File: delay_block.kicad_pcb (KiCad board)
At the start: 2 copper layers, 55.4 x 81.8 mm, 51 parts, among them J1 Conn_Coaxial, J2 Conn_Coaxial, J3 Conn_Coaxial, J4 Conn_Coaxial, J5 Conn_Coaxial, J6 Conn_Coaxial, J7 Conn_Coaxial, J8 Conn_Coaxial, J9 Screw_Terminal_01x02, U1 DS1100Z-500+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

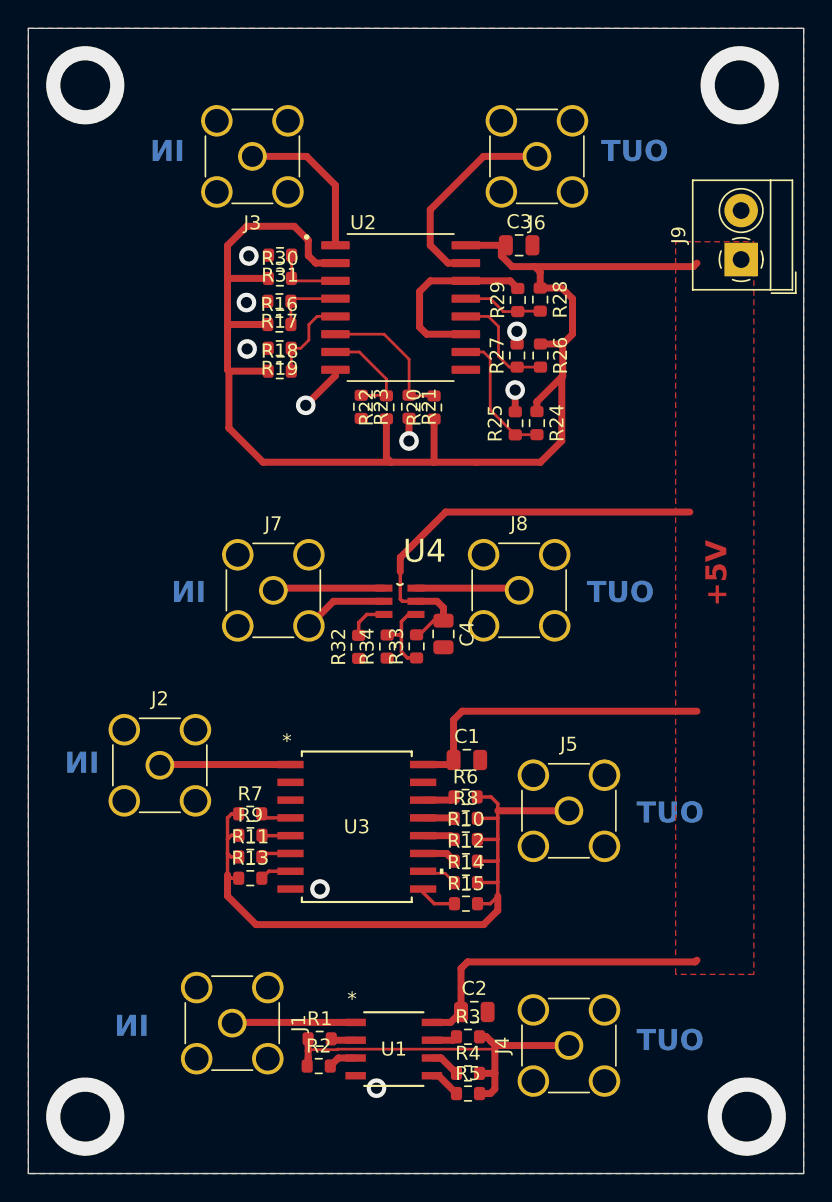
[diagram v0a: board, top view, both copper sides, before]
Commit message: hardwired jumpers to set ~500us everywhere
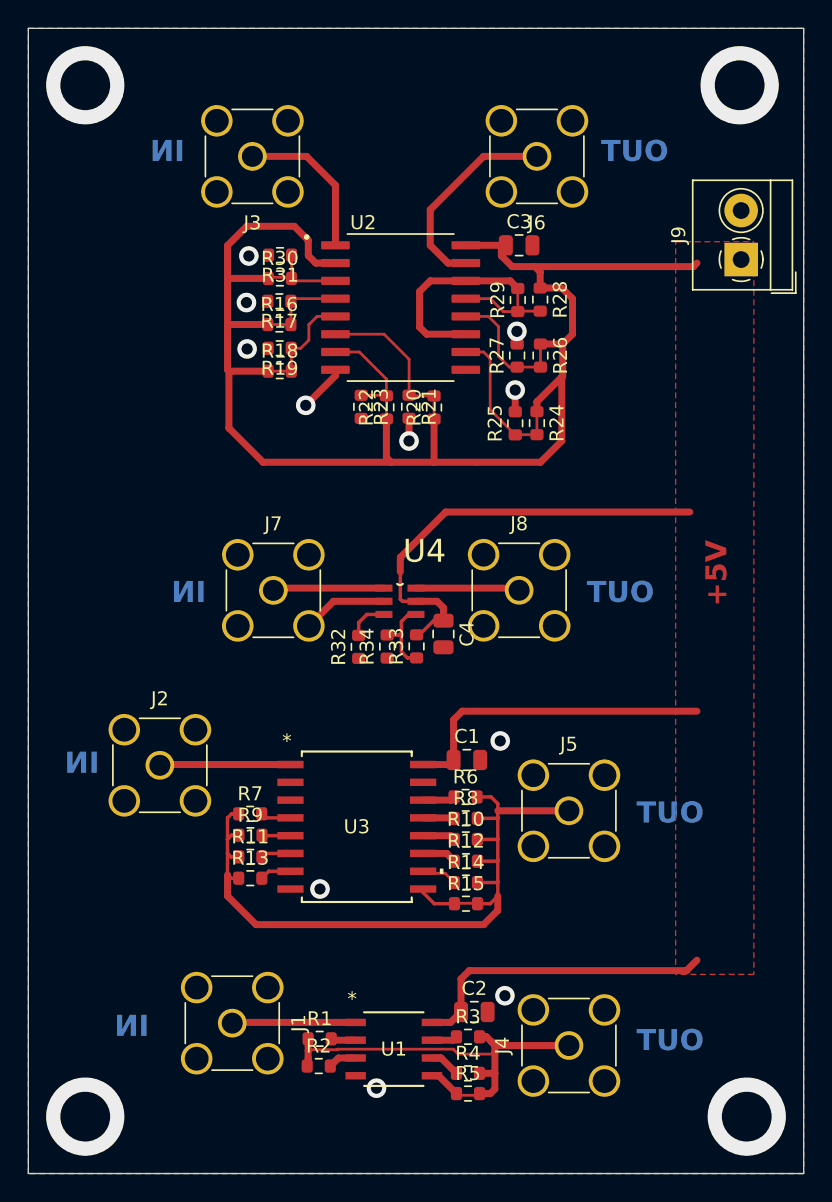
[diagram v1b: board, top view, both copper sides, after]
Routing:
- net GND: vias 13 -> 15
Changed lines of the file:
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@@
 		)
+	)
+	(gr_line
+		(start 106.193742 91.315606)
+		(end 106.188841 89.839156)
+		(stroke
+			(width 0.2)
+			(type default)
+		)
+		(layer "F.Cu")
+	)
+	(gr_line
+		(start 94.433714 87.98479)
+		(end 95.910164 87.979889)
+		(stroke
+			(width 0.2)
+			(type default)
+		)
+		(layer "F.Cu")
+	)
+	(gr_line
+		(start 107.696 139.7)
+		(end 109.728 139.7)
+		(stroke
+			(width 0.2)
+			(type default)
+		)
+		(layer "F.Cu")
+	)
+	(gr_line
+		(start 107.696 125.984)
+		(end 109.22 125.984)
+		(stroke
+			(width 0.2)
+			(type default)
+		)
+		(layer "F.Cu")
+	)
+	(gr_line
+		(start 112.171951 83.640874)
+		(end 112.16705 82.164424)
+		(stroke
+			(width 0.2)
+			(type default)
+		)
+		(layer "F.Cu")
+	)
+	(gr_line
+		(start 113.54045 92.432225)
+		(end 113.535549 90.955775)
+		(stroke
+			(width 0.2)
+			(type default)
+		)
+		(layer "F.Cu")
+	)
+	(gr_line
+		(start 113.79445 87.606225)
+		(end 113.789549 86.129775)
+		(stroke
+			(width 0.2)
+			(type default)
+		)
+		(layer "F.Cu")
+	)
+	(gr_line
+		(start 94.403323 84.65273)
+		(end 95.879773 84.647829)
+		(stroke
+			(width 0.2)
+			(type default)
+		)
+		(layer "F.Cu")
+	)
+	(gr_line
+		(start 94.488 81.28)
+		(end 95.96445 81.275099)
+		(stroke
+			(width 0.2)
+			(type default)
+		)
+		(layer "F.Cu")
+	)
+	(gr_line
+		(start 102.789702 91.305102)
+		(end 102.784801 89.828652)
+		(stroke
+			(width 0.2)
+			(type default)
+		)
+		(layer "F.Cu")
 	)
 	(gr_rect
@@
 	)
 	(via
+		(at 111.252 132.588)
+		(size 1.4)
+		(drill 0.8)
+		(layers "F.Cu" "B.Cu")
+		(free yes)
+		(net 5)
+	)
+	(via
 		(at 104.404031 92.968017)
 		(size 1.4)
@@
 	)
 	(via
+		(at 110.917719 114.392297)
+		(size 1.4)
+		(drill 0.8)
+		(layers "F.Cu" "B.Cu")
+		(free yes)
+		(net 5)
+	)
+	(via
 		(at 128.016 67.564)
 		(size 5.588)
@@
 	)
 	(segment
+		(start 108.712 130.795203)
+		(end 124.220797 130.795203)
+		(width 0.5)
+		(layer "F.Cu")
+		(net 6)
+	)
+	(segment
 		(start 91.520515 81.360515)
 		(end 91.44 81.28)
@@
 	)
 	(segment
-		(start 108.116192 130.643808)
-		(end 108.586202 130.173798)
-		(width 0.5)
-		(layer "F.Cu")
-		(net 6)
-	)
-	(segment
 		(start 115.319944 82.045944)
 		(end 113.772173 82.045944)
@@
 	)
 	(segment
+		(start 108.116192 133.749203)
+		(end 108.116192 131.391011)
+		(width 0.5)
+		(layer "F.Cu")
+		(net 6)
+	)
+	(segment
 		(start 91.44 84.836)
 		(end 91.44 83.82)
@@
 	)
 	(segment
+		(start 108.116192 131.391011)
+		(end 108.712 130.795203)
+		(width 0.5)
+		(layer "F.Cu")
+		(net 6)
+	)
+	(segment
 		(start 105.41 116.078)
 		(end 107.25909 116.078)
@@
 	)
 	(segment
-		(start 124.842202 130.173798)
+		(start 124.220797 130.795203)
 		(end 124.968 130.048)
 		(width 0.5)
@@
 	)
 	(segment
-		(start 108.586202 130.173798)
-		(end 124.842202 130.173798)
-		(width 0.5)
-		(layer "F.Cu")
-		(net 6)
-	)
-	(segment
 		(start 116.078 82.804)
 		(end 115.319944 82.045944)
@@
 	)
 	(segment
-		(start 108.116192 133.749203)
-		(end 108.116192 130.643808)
-		(width 0.5)
-		(layer "F.Cu")
-		(net 6)
-	)
-	(segment
 		(start 105.14958 106.813788)
 		(end 104.93911 106.813788)
@@
 	)
 	(segment
+		(start 107.913347 136.757326)
+		(end 110.428262 136.757326)
+		(width 0.2)
+		(layer "F.Cu")
+		(net 10)
+	)
+	(segment
 		(start 97.197378 137.545617)
 		(end 97.131311 137.611684)
@@
 	)
 	(segment
+		(start 97.197378 136.514955)
+		(end 97.270028 136.442305)
+		(width 0.2)
+		(layer "F.Cu")
+		(net 10)
+	)
+	(segment
 		(start 110.533588 136.373461)
 		(end 110.503204 136.403845)
@@
 	)
 	(segment
+		(start 107.559866 136.403845)
+		(end 107.913347 136.757326)
+		(width 0.2)
+		(layer "F.Cu")
+		(net 10)
+	)
+	(segment
+		(start 110.533588 136.652)
+		(end 110.533588 136.1157)
+		(width 0.5)
+		(layer "F.Cu")
+		(net 10)
+	)
+	(segment
+		(start 99.298486 136.403845)
+		(end 107.559866 136.403845)
+		(width 0.2)
+		(layer "F.Cu")
+		(net 10)
+	)
+	(segment
 		(start 110.213077 139.575691)
 		(end 110.533588 139.25518)
@@
 	)
 	(segment
+		(start 110.428262 136.757326)
+		(end 110.533588 136.652)
+		(width 0.2)
+		(layer "F.Cu")
+		(net 10)
+	)
+	(segment
+		(start 97.270028 136.442305)
+		(end 99.260026 136.442305)
+		(width 0.2)
+		(layer "F.Cu")
+		(net 10)
+	)
+	(segment
 		(start 115.824 136.144)
 		(end 110.561889 136.144)
@@
 	)
 	(segment
+		(start 99.260026 136.442305)
+		(end 99.298486 136.403845)
+		(width 0.2)
+		(layer "F.Cu")
+		(net 10)
+	)
+	(segment
 		(start 110.533588 136.1157)
 		(end 110.270943 135.853054)
@@
 	)
 	(segment
-		(start 97.270028 136.442305)
-		(end 97.197378 136.514955)
-		(width 0.2)
-		(layer "F.Cu")
-		(net 10)
-	)
-	(segment
-		(start 110.503204 136.403845)
-		(end 99.298486 136.403845)
-		(width 0.2)
-		(layer "F.Cu")
-		(net 10)
-	)
-	(segment
-		(start 110.533588 138.131677)
-		(end 110.533588 136.1157)
-		(width 0.5)
-		(layer "F.Cu")
-		(net 10)
-	)
-	(segment
 		(start 109.438609 138.131677)
 		(end 110.533588 138.131677)
@@
 	)
 	(segment
-		(start 99.298486 136.403845)
-		(end 99.260026 136.442305)
-		(width 0.2)
-		(layer "F.Cu")
-		(net 10)
-	)
-	(segment
 		(start 97.197378 135.667305)
 		(end 97.197378 136.514955)
@@
 	)
 	(segment
-		(start 99.260026 136.442305)
-		(end 97.270028 136.442305)
-		(width 0.2)
+		(start 110.533588 138.131677)
+		(end 110.533588 136.652)
+		(width 0.5)
 		(layer "F.Cu")
 		(net 10)
@@
 		(hatch edge 0.5)
 		(connect_pads
-			(clearance 1)
+			(clearance 0.75)
 		)
 		(min_thickness 0.25)

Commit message: Added attributes DNP
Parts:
- R32: value 0 -> 49.9k
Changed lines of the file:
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@@
 		(sheetname "Root")
 		(sheetfile "delay_block.kicad_sch")
-		(attr smd)
+		(attr smd dnp)
 		(fp_line
 			(start -0.237258 -0.5225)
@@
 		(sheetname "Root")
 		(sheetfile "delay_block.kicad_sch")
-		(attr smd)
+		(attr smd dnp)
 		(fp_line
 			(start -0.237258 -0.5225)
@@
 		(sheetname "Root")
 		(sheetfile "delay_block.kicad_sch")
-		(attr smd)
+		(attr smd dnp)
 		(fp_line
 			(start -0.237258 -0.5225)
@@
 		(sheetname "Root")
 		(sheetfile "delay_block.kicad_sch")
-		(attr smd)
+		(attr smd dnp)
 		(fp_line
 			(start -0.237258 -0.5225)
@@
 		(sheetname "Root")
 		(sheetfile "delay_block.kicad_sch")
-		(attr smd)
+		(attr smd dnp)
 		(fp_line
 			(start -0.237258 0.5225)
@@
 		(sheetname "Root")
 		(sheetfile "delay_block.kicad_sch")
-		(attr smd)
+		(attr smd dnp)
 		(fp_line
 			(start -0.237258 -0.5225)
@@
 		(sheetname "Root")
 		(sheetfile "delay_block.kicad_sch")
-		(attr smd)
+		(attr smd dnp)
 		(fp_line
 			(start -0.237258 -0.5225)
@@
 		(sheetname "Root")
 		(sheetfile "delay_block.kicad_sch")
-		(attr smd)
+		(attr smd dnp)
 		(fp_line
 			(start -0.237258 0.5225)
@@
 		(sheetname "Root")
 		(sheetfile "delay_block.kicad_sch")
-		(attr smd)
+		(attr smd dnp)
 		(fp_line
 			(start -0.237258 -0.5225)
@@
 		(sheetname "Root")
 		(sheetfile "delay_block.kicad_sch")
-		(attr smd)
+		(attr smd dnp)
 		(fp_line
 			(start -0.237258 -0.5225)
@@
 			)
 		)
-		(property "Value" "0"
+		(property "Value" "49.9k"
 			(at 0 1.43 90)
 			(layer "F.Fab")
@@
 		(sheetname "Root")
 		(sheetfile "delay_block.kicad_sch")
-		(attr smd)
+		(attr smd dnp)
 		(fp_line
 			(start -0.237258 -0.5225)
@@
 		(sheetname "Root")
 		(sheetfile "delay_block.kicad_sch")
-		(attr smd)
+		(attr smd dnp)
 		(fp_line
 			(start -0.237258 0.5225)
@@
 		(sheetname "Root")
 		(sheetfile "delay_block.kicad_sch")
-		(attr smd)
+		(attr smd dnp)
 		(fp_line
 			(start -0.237258 -0.5225)
@@
 		(sheetname "Root")
 		(sheetfile "delay_block.kicad_sch")
-		(attr smd)
+		(attr smd dnp)
 		(fp_line
 			(start -0.237258 -0.5225)
@@
 		(sheetname "Root")
 		(sheetfile "delay_block.kicad_sch")
-		(attr smd)
+		(attr smd dnp)
 		(fp_line
 			(start -0.237258 -0.5225)
@@
 		(sheetname "Root")
 		(sheetfile "delay_block.kicad_sch")
-		(attr smd)
+		(attr smd dnp)
 		(fp_line
 			(start -0.237258 0.5225)
@@
 		(sheetname "Root")
 		(sheetfile "delay_block.kicad_sch")
-		(attr smd)
+		(attr smd dnp)
 		(fp_line
 			(start -0.237258 -0.5225)
@@
 		(sheetname "Root")
 		(sheetfile "delay_block.kicad_sch")
-		(attr smd)
+		(attr smd dnp)
 		(fp_line
 			(start -0.237258 -0.5225)
@@
 		(sheetname "Root")
 		(sheetfile "delay_block.kicad_sch")
-		(attr smd)
+		(attr smd dnp)
 		(fp_line
 			(start -0.237258 -0.5225)
@@
 		(sheetname "Root")
 		(sheetfile "delay_block.kicad_sch")
-		(attr smd)
+		(attr smd dnp)
 		(fp_line
 			(start -0.237258 -0.5225)
@@
 		(sheetname "Root")
 		(sheetfile "delay_block.kicad_sch")
-		(attr smd)
+		(attr smd dnp)
 		(fp_line
 			(start -0.237258 -0.5225)
@@
 		(sheetname "Root")
 		(sheetfile "delay_block.kicad_sch")
-		(attr smd)
+		(attr smd dnp)
 		(fp_line
 			(start -0.237258 -0.5225)
@@
 		(sheetname "Root")
 		(sheetfile "delay_block.kicad_sch")
-		(attr smd)
+		(attr smd dnp)
 		(fp_line
 			(start -0.237258 0.5225)
@@
 		(fp_text user "*"
 			(at -1.6129 -2.4257 0)
+			(unlocked yes)
 			(layer "F.Fab")
 			(effects
@@
 			)
 		)
-		(fp_text user "*"
-			(at -1.6129 -2.4257 0)
+		(fp_text user "${REFERENCE}"
+			(at 0 0 0)
 			(unlocked yes)
 			(layer "F.Fab")
@@
 			)
 		)
-		(fp_text user "${REFERENCE}"
-			(at 0 0 0)
-			(unlocked yes)
+		(fp_text user "*"
+			(at -1.6129 -2.4257 0)
 			(layer "F.Fab")
 			(effects
@@
 		(sheetname "Root")
 		(sheetfile "delay_block.kicad_sch")
-		(attr smd)
+		(attr smd dnp)
 		(fp_line
 			(start -0.237258 0.5225)
@@
 		(sheetname "Root")
 		(sheetfile "delay_block.kicad_sch")
-		(attr smd)
+		(attr smd dnp)
 		(fp_line
 			(start -0.237258 0.5225)
@@
 		(sheetname "Root")
 		(sheetfile "delay_block.kicad_sch")
-		(attr smd)
+		(attr smd dnp)
 		(fp_line
 			(start -0.237258 -0.5225)
@@
 		(fp_text user "*"
 			(at -4.9911 -6.1214 0)
-			(unlocked yes)
 			(layer "F.SilkS")
 			(effects
@@
 		(fp_text user "*"
 			(at -4.9911 -6.1214 0)
+			(unlocked yes)
 			(layer "F.SilkS")
 			(effects
@@
 		(fp_text user "*"
 			(at -3.4163 -5.1689 0)
+			(unlocked yes)
 			(layer "F.Fab")
 			(effects
@@
 			)
 		)
-		(fp_text user "${REFERENCE}"
-			(at 0 0 0)
-			(unlocked yes)
+		(fp_text user "*"
+			(at -3.4163 -5.1689 0)
 			(layer "F.Fab")
 			(effects
@@
 			)
 		)
-		(fp_text user "*"
-			(at -3.4163 -5.1689 0)
+		(fp_text user "${REFERENCE}"
+			(at 0 0 0)
 			(unlocked yes)
 			(layer "F.Fab")
@@
 		(sheetname "Root")
 		(sheetfile "delay_block.kicad_sch")
-		(attr smd)
+		(attr smd dnp)
 		(fp_line
 			(start -0.237258 -0.5225)
@@
 		(sheetname "Root")
 		(sheetfile "delay_block.kicad_sch")
-		(attr smd)
+		(attr smd dnp)
 		(fp_line
 			(start -0.237258 -0.5225)
@@
 		(sheetname "Root")
 		(sheetfile "delay_block.kicad_sch")
-		(attr smd)
+		(attr smd dnp)
 		(fp_line
 			(start -0.237258 -0.5225)
@@
 		(sheetname "Root")
 		(sheetfile "delay_block.kicad_sch")
-		(attr smd)
+		(attr smd dnp)
 		(fp_line
 			(start -0.237258 -0.5225)
@@
 		(sheetname "Root")
 		(sheetfile "delay_block.kicad_sch")
-		(attr smd)
+		(attr smd dnp)
 		(fp_line
 			(start -0.237258 0.5225)
@@
 		(sheetname "Root")
 		(sheetfile "delay_block.kicad_sch")
-		(attr smd)
+		(attr smd dnp)
 		(fp_line
 			(start -0.237258 -0.5225)
